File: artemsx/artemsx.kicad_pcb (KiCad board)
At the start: 2 copper layers, 87 parts, among them J1 PS2_CONN, J2 MSX_Slot, J3 MSX_Slot, J4 CONN_JOY, J5 CONN_JOY, U1 74HC32, U10 TMS99x8, U11 74HCT244, U12 74HCT244, U13 74HCT245, U14 74HCT244, U15 74HC74, U16 74HC08, U17 74HC32, U18 Z84C00, U19 82C55A, U2 74HC04, U20 74HC153, U21 74HC139, U23 74HC138, U24 74HC32, U25 SST39SF0x0, U26 ATMEGA328P, U27 74HC154, U28 74HC595, U29 74HC595, U3 HM62256ALP-10, U30 74HC595, U31 74HC595, U32 74HC595, U33 74HC595, U34 74HC595, U35 74HC595, U36 74HC595, U37 74HC595, U38 4069, U39 74HC07, U4 HM62256ALP-10, U40 74HC74, U41 AY-3-8910, U42 74HC157, U43 74HC157, U44 74HC32, U45 74HC595, U5 74HCT04, U6 74HCT574, U7 74HCT574, U8 74HCT574, U9 HM62256ALP-10, Y1 10.7386Mhz, Y2 16Mhz, Y3 3.58Mhz

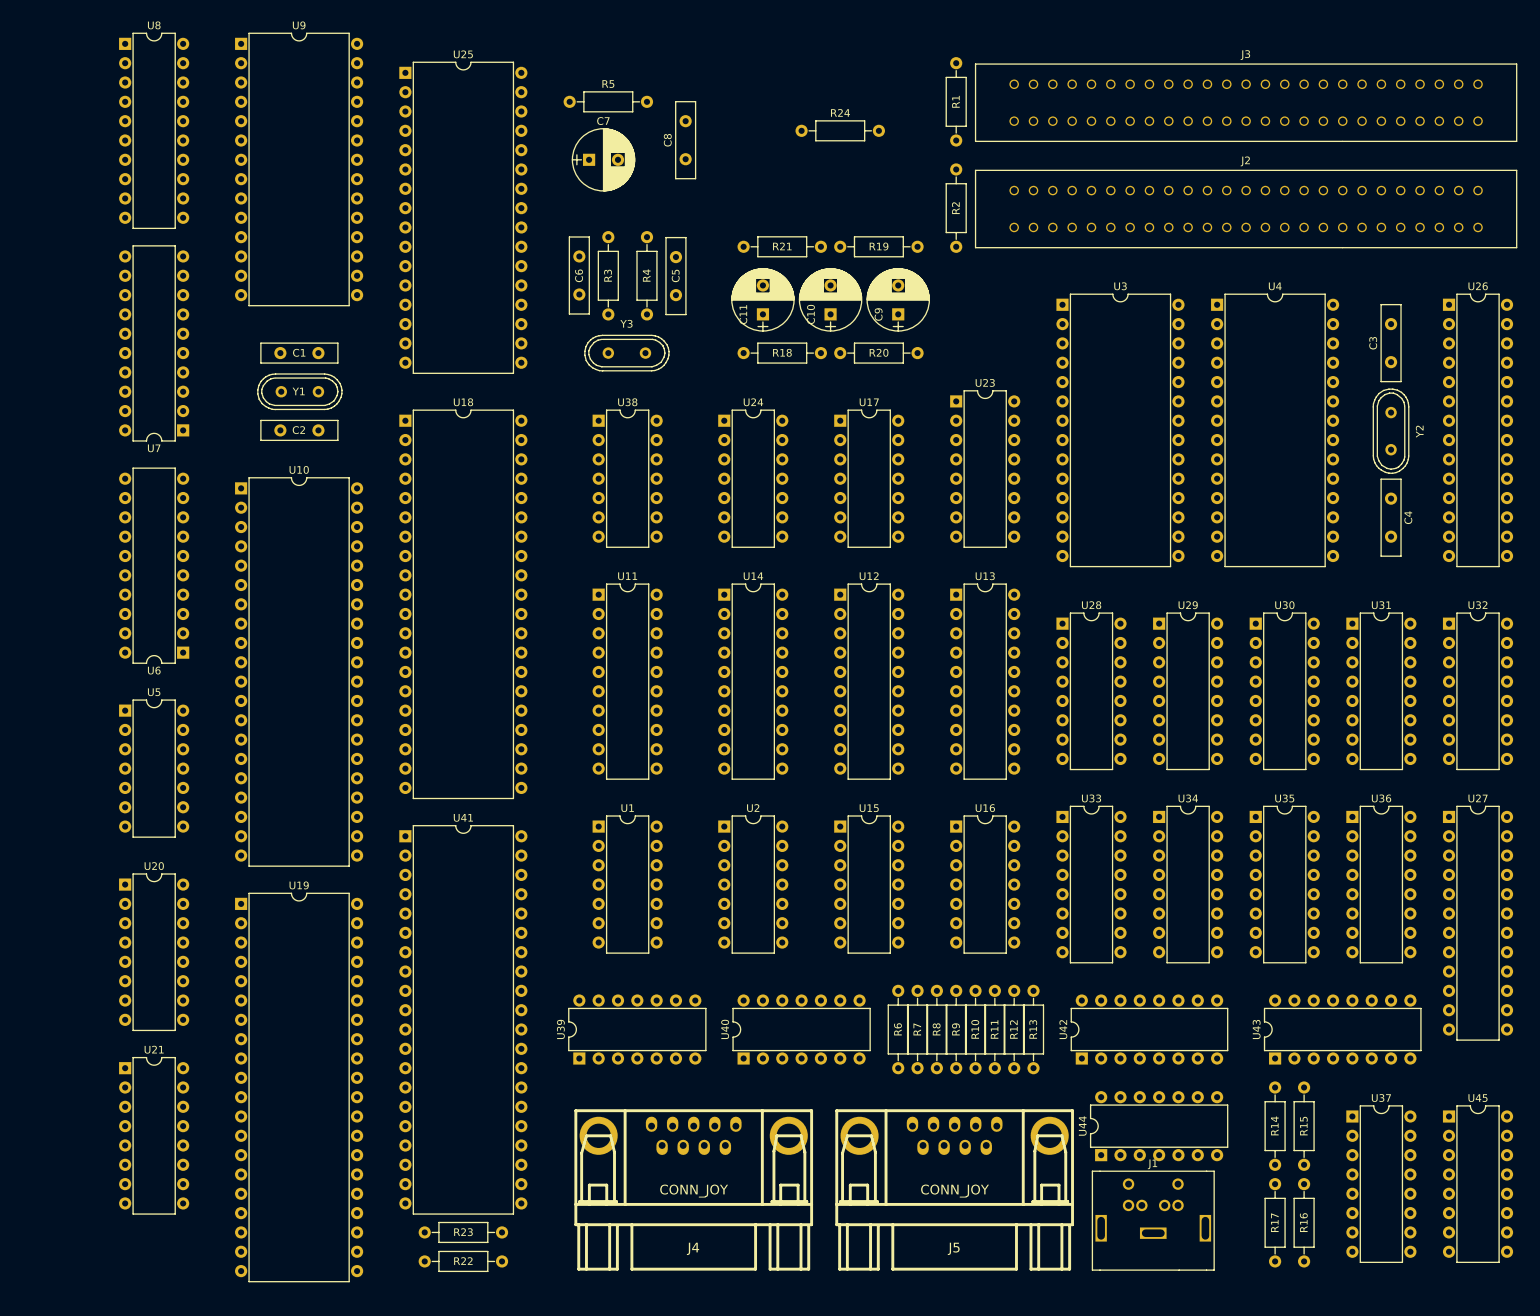
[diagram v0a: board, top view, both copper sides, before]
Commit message: Include power connector & decoupling caps to the PCB
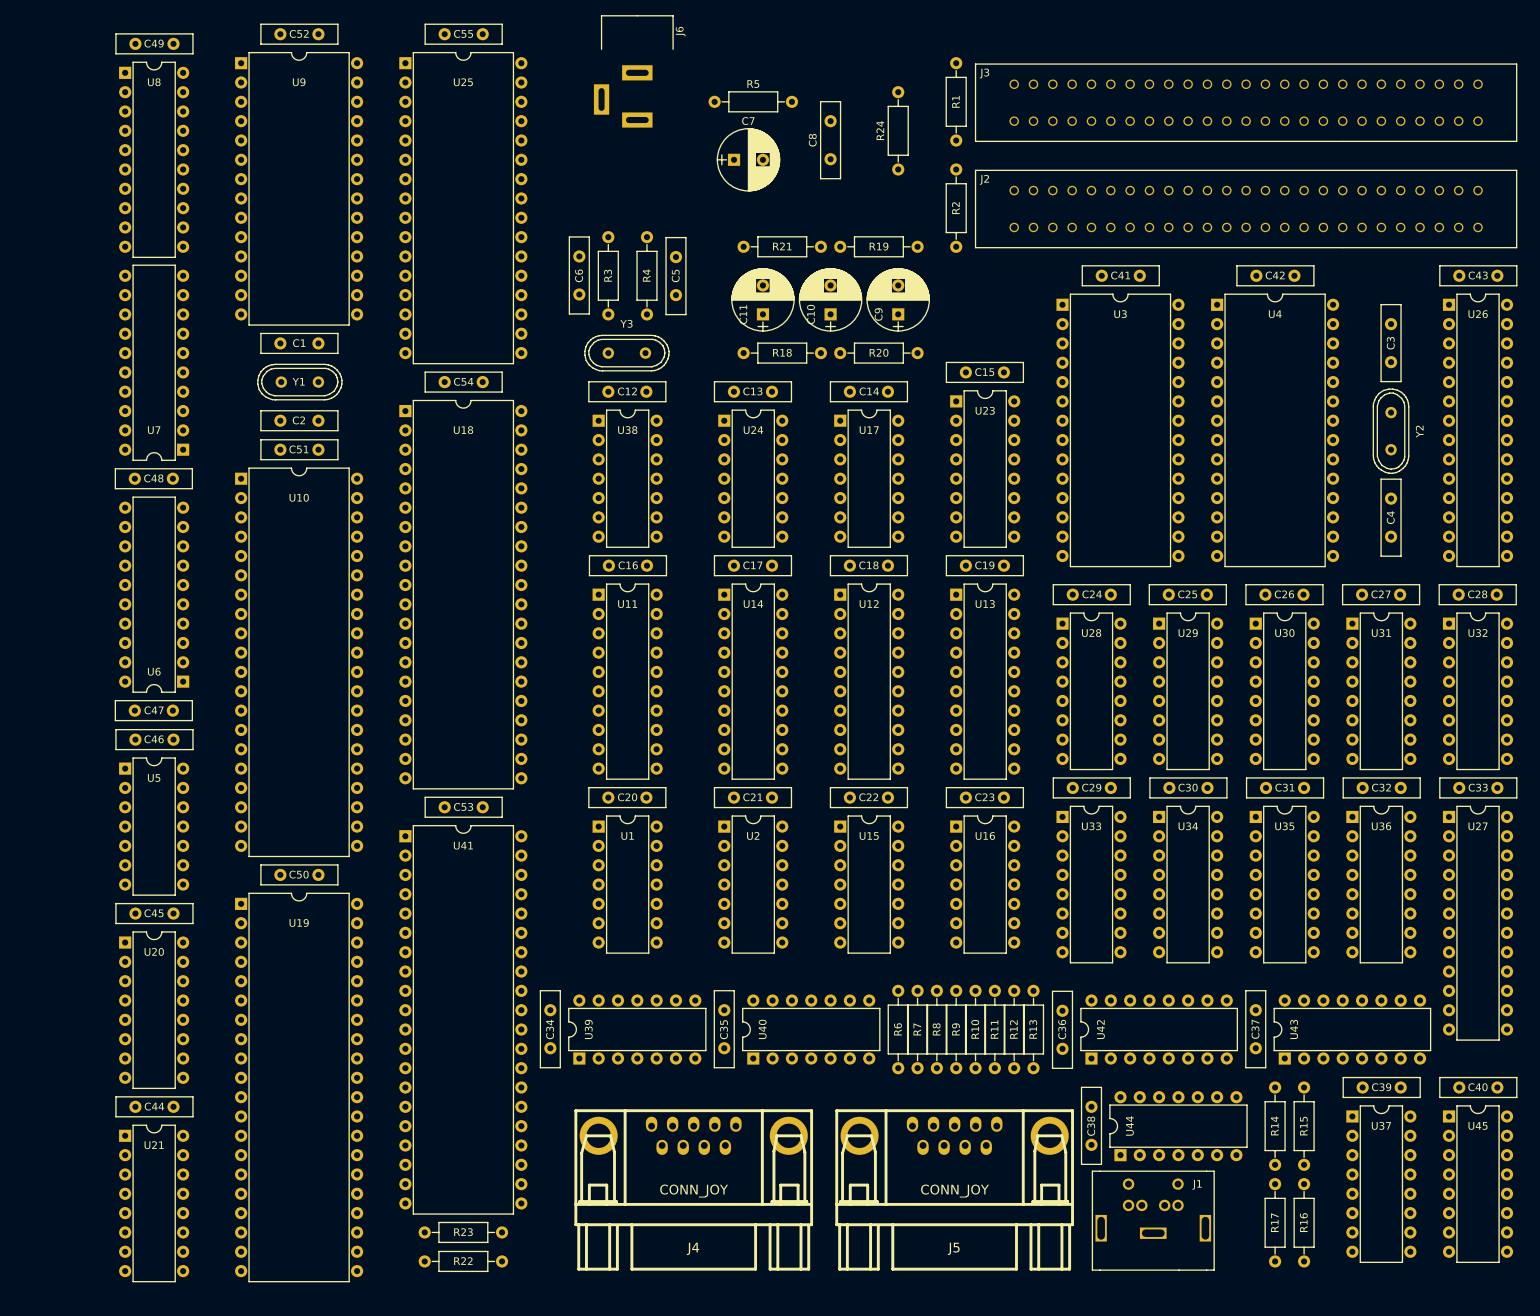
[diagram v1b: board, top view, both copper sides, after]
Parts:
- added C12: 22pF, artemsx:Disc_capacitor, F.Cu at (176.4, 92.7)
- added C13: 22pF, artemsx:Disc_capacitor, F.Cu at (193.0, 92.7)
- added C14: 22pF, artemsx:Disc_capacitor, F.Cu at (208.2, 92.7)
- added C15: 22pF, artemsx:Disc_capacitor, F.Cu at (223.4, 90.2)
- added C16: 22pF, artemsx:Disc_capacitor, F.Cu at (176.5, 115.6)
- added C17: 22pF, artemsx:Disc_capacitor, F.Cu at (193.0, 115.6)
- added C18: 22pF, artemsx:Disc_capacitor, F.Cu at (208.2, 115.6)
- added C19: 22pF, artemsx:Disc_capacitor, F.Cu at (223.4, 115.6)
- added C20: 22pF, artemsx:Disc_capacitor, F.Cu at (176.4, 146.1)
- added C21: 22pF, artemsx:Disc_capacitor, F.Cu at (193.0, 146.1)
- added C22: 22pF, artemsx:Disc_capacitor, F.Cu at (208.2, 146.1)
- added C23: 22pF, artemsx:Disc_capacitor, F.Cu at (223.4, 146.1)
- added C24: 22pF, artemsx:Disc_capacitor, F.Cu at (237.5, 119.4)
- added C25: 22pF, artemsx:Disc_capacitor, F.Cu at (250.1, 119.4)
- added C26: 22pF, artemsx:Disc_capacitor, F.Cu at (262.8, 119.4)
- added C27: 22pF, artemsx:Disc_capacitor, F.Cu at (275.5, 119.4)
- added C28: 22pF, artemsx:Disc_capacitor, F.Cu at (288.2, 119.4)
- added C29: 22pF, artemsx:Disc_capacitor, F.Cu at (237.5, 144.8)
- added C30: 22pF, artemsx:Disc_capacitor, F.Cu at (250.2, 144.8)
- added C31: 22pF, artemsx:Disc_capacitor, F.Cu at (262.9, 144.8)
- added C32: 22pF, artemsx:Disc_capacitor, F.Cu at (275.6, 144.8)
- added C33: 22pF, artemsx:Disc_capacitor, F.Cu at (288.3, 144.8)
- added C34: 22pF, artemsx:Disc_capacitor, F.Cu at (163.8, 174.0)
- added C35: 22pF, artemsx:Disc_capacitor, F.Cu at (186.7, 174.0)
- added C36: 22pF, artemsx:Disc_capacitor, F.Cu at (231.1, 174.1)
- added C37: 22pF, artemsx:Disc_capacitor, F.Cu at (256.5, 174.0)
- added C38: 22pF, artemsx:Disc_capacitor, F.Cu at (234.9, 186.7)
- added C39: 22pF, artemsx:Disc_capacitor, F.Cu at (275.6, 184.2)
- added C40: 22pF, artemsx:Disc_capacitor, F.Cu at (288.3, 184.2)
- added C41: 22pF, artemsx:Disc_capacitor, F.Cu at (241.3, 77.5)
- added C42: 22pF, artemsx:Disc_capacitor, F.Cu at (261.6, 77.5)
- added C43: 22pF, artemsx:Disc_capacitor, F.Cu at (288.3, 77.5)
- added C44: 22pF, artemsx:Disc_capacitor, F.Cu at (114.3, 186.7)
- added C45: 22pF, artemsx:Disc_capacitor, F.Cu at (114.3, 161.3)
- added C46: 22pF, artemsx:Disc_capacitor, F.Cu at (114.3, 138.4)
- added C47: 22pF, artemsx:Disc_capacitor, F.Cu at (109.2, 134.6)
- added C48: 22pF, artemsx:Disc_capacitor, F.Cu at (109.2, 104.1)
- added C49: 22pF, artemsx:Disc_capacitor, F.Cu at (114.3, 47.0)
- added C50: 22pF, artemsx:Disc_capacitor, F.Cu at (133.3, 156.2)
- added C51: 22pF, artemsx:Disc_capacitor, F.Cu at (133.3, 100.3)
- added C52: 22pF, artemsx:Disc_capacitor, F.Cu at (133.3, 45.7)
- added C53: 22pF, artemsx:Disc_capacitor, F.Cu at (154.9, 147.3)
- added C54: 22pF, artemsx:Disc_capacitor, F.Cu at (154.9, 91.4)
- added C55: 22pF, artemsx:Disc_capacitor, F.Cu at (154.9, 45.7)
- added J6: PWR_conn, artemsx:Jack_55_21, F.Cu at (170.6, 54.3)
- moved C7 19.1 mm to (188.0, 62.2)
- moved C8 19.0 mm to (200.7, 62.1)
- moved R5 19.0 mm to (185.4, 54.6)
- moved R24 13.7 mm to (209.6, 63.5), turned to 90 degrees
- moved U21 8.89 mm to (108.0, 190.5)
- moved U20 7.62 mm to (108.0, 165.1)
- moved U5 7.62 mm to (108.0, 142.2)
- moved U6 3.81 mm to (115.6, 130.8)
- moved U8 3.81 mm to (108.0, 50.8)
- moved U9 2.54 mm to (123.2, 49.5)
- moved U44 2.54 mm to (238.8, 193.0)
- moved U7 2.54 mm to (115.6, 100.3)
- moved U43 1.27 mm to (260.4, 180.3)
- moved C2 1.27 mm to (128.3, 96.5)
- moved U40 1.27 mm to (190.5, 180.3)
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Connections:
- J2 pad 48: +12VA -> GND
- J2 pad 50: -12VA -> GND
- J3 pad 48: +12VA -> GND
- J3 pad 50: -12VA -> GND

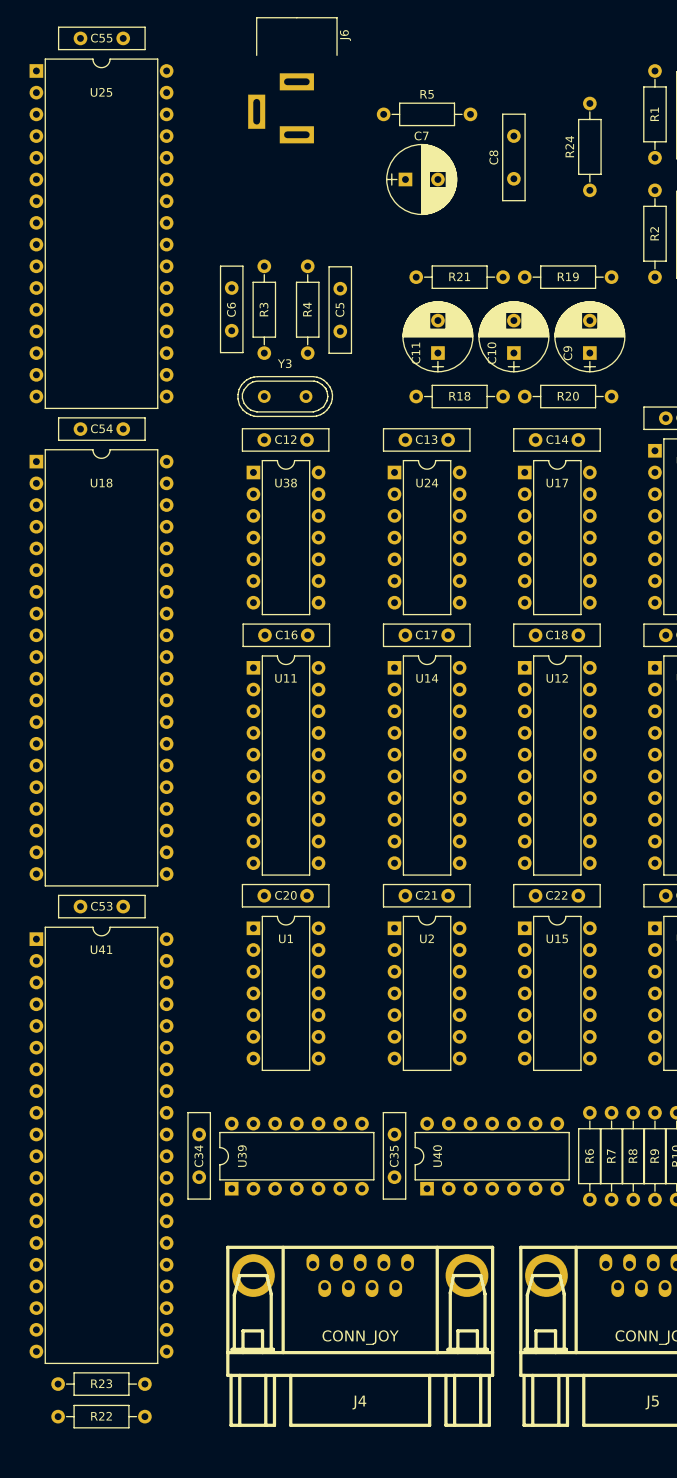
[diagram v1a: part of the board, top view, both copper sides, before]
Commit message: Replace the footprint of the electrolytic caps
And also the 3D shape.
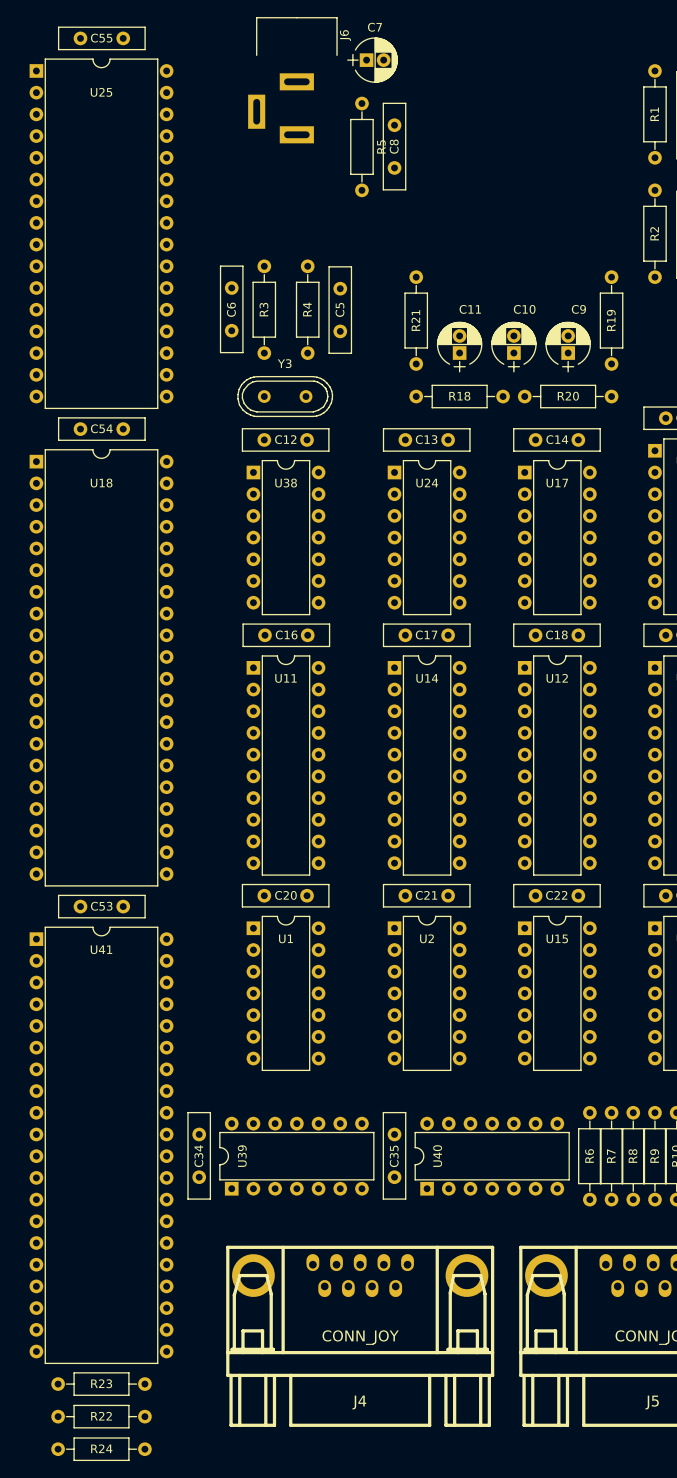
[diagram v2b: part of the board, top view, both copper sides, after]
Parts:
- moved R24 156.3 mm to (157.5, 210.8), turned to 180 degrees
- moved C7 14.7 mm to (183.4, 48.3)
- moved C8 14.0 mm to (186.7, 60.9)
- moved R21 10.2 mm to (189.2, 83.8), turned to 90 degrees
- moved R22 10.2 mm to (147.3, 207.0), turned to 0 degrees
- moved R23 10.2 mm to (147.3, 203.2), turned to 0 degrees
- moved R5 2.84 mm to (182.9, 53.3), turned to 270 degrees
- moved C9 2.54 mm to (207.0, 82.5)
- moved C11 2.54 mm to (194.3, 82.5)
- turned R19 to 270 degrees
